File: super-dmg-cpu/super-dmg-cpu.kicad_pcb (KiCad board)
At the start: 2 copper layers, 83 x 78.5 mm, 61 parts, among them CN1 SCREEN, CN2 CART, CN3 BATTERY, CN4 BATTERY, P1 CART SHIELD GND PADS, P2 GND PAD, P3 GND PAD, P4 GND PAD, SW1 DPDT, U1 CPU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

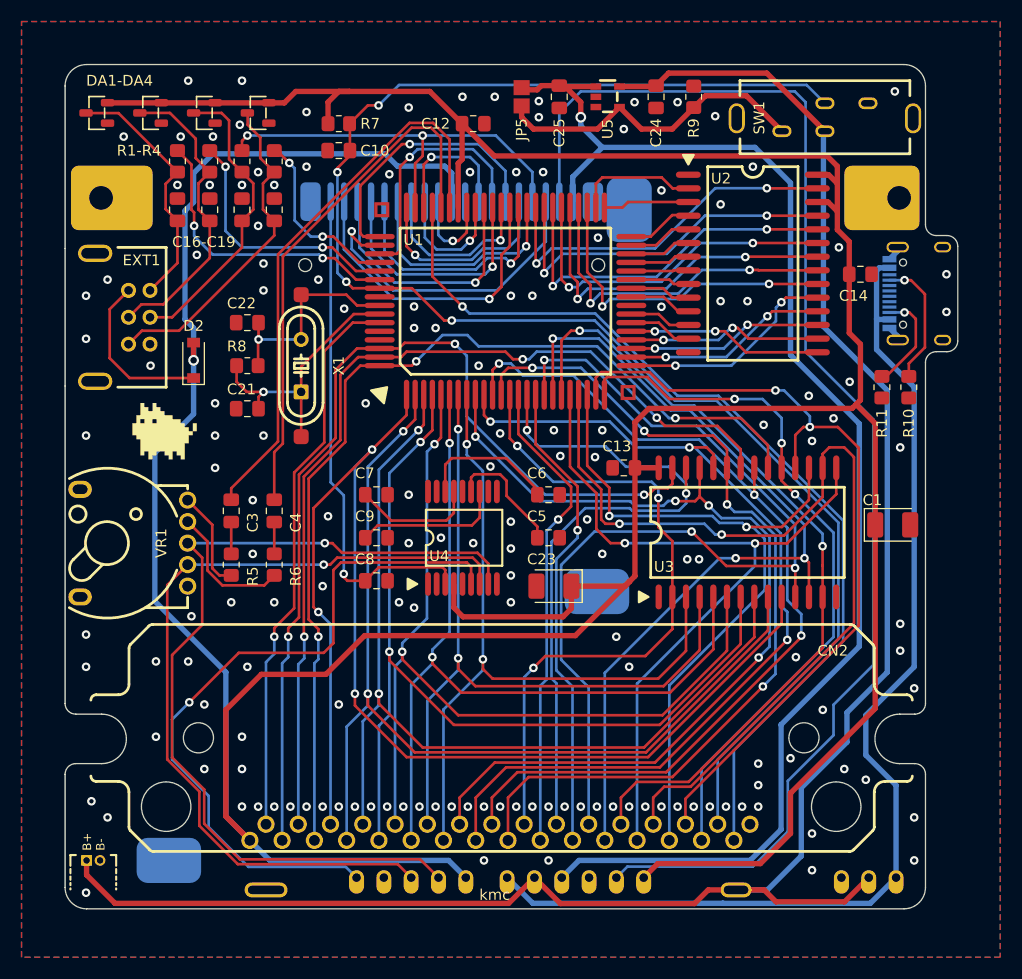
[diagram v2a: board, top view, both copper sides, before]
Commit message: CPU: clean up for DRC
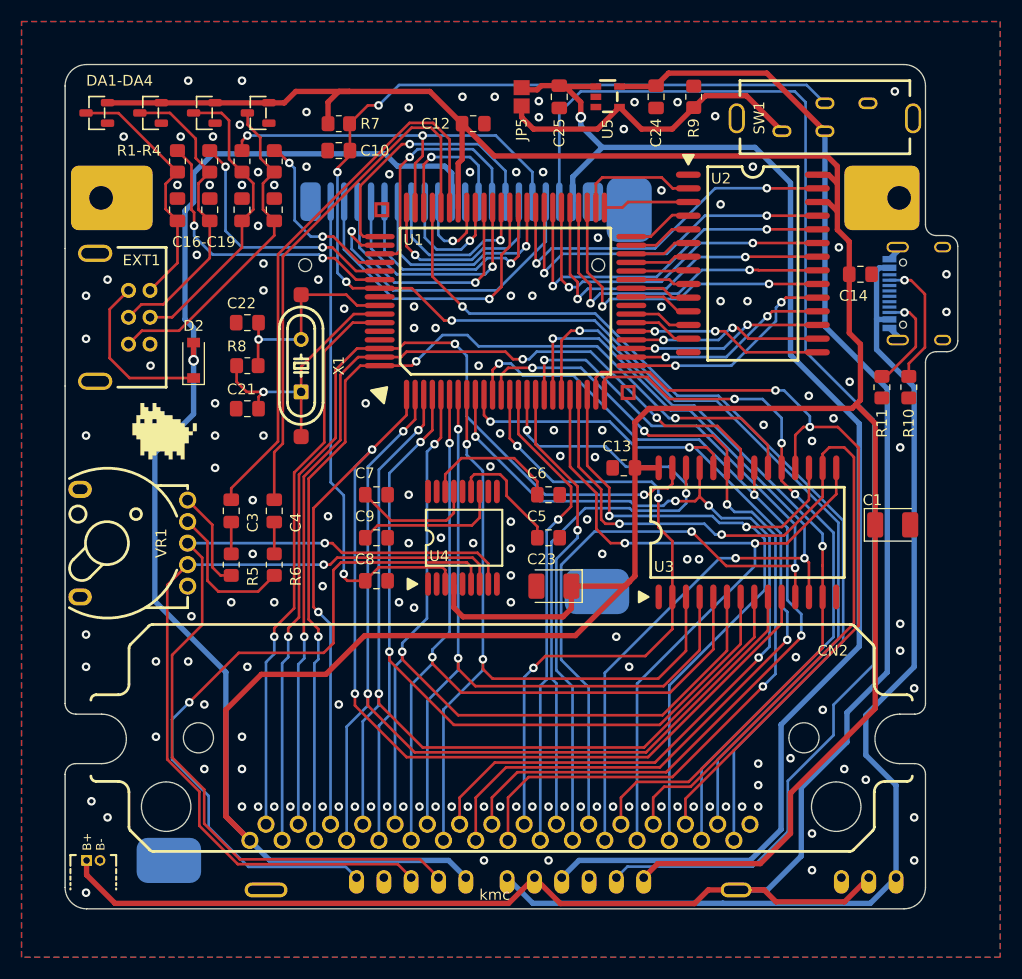
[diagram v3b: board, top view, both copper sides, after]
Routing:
- net Net-(R6-Pad2): track 12.5 -> 13.5 mm
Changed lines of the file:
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@@
     (fp_line (start -6 5) (end -5.031 5) (layer "F.SilkS") (width 0.254))
     (fp_arc (start -2.5 4) (mid -6.581538 -0.183962) (end -6 -6) (layer "F.SilkS") (width 0.254))
-    (fp_arc (start 6 -6) (mid 6.581539 -0.183961) (end 2.5 4) (layer "F.SilkS") (width 0.254))
+    (fp_arc (start 6 -6) (mid 6.581539 -0.183962) (end 2.5 4) (layer "F.SilkS") (width 0.254))
     (fp_arc (start -3.199638 -4.100525) (mid -3.096245 -5.695327) (end -1.501 -5.599) (layer "F.SilkS") (width 0.254))
     (fp_circle (center 0 -2.5) (end 2 -2.5) (layer "F.SilkS") (width 0.254) (fill none))
@@
   (segment (start 105.503135 49.651323) (end 105.501323 49.651323) (width 0.5) (layer "B.Cu") (net 16))
   (segment (start 105.551812 49.7) (end 105.503135 49.651323) (width 0.5) (layer "B.Cu") (net 16))
-  (segment (start 40 90.418296) (end 42.986489 93.404785) (width 0.25) (layer "F.Cu") (net 17))
-  (segment (start 42.8 78.1) (end 40 80.9) (width 0.25) (layer "F.Cu") (net 17))
-  (segment (start 41.445597 70.5) (end 42.8 71.854403) (width 0.25) (layer "F.Cu") (net 17))
-  (segment (start 63.07 99.9) (end 64.77 101.6) (width 0.25) (layer "F.Cu") (net 17))
   (segment (start 55.8 71.4) (end 68.4 71.4) (width 0.25) (layer "F.Cu") (net 17))
   (segment (start 69.4 72.4) (end 69.4 74.3) (width 0.25) (layer "F.Cu") (net 17))
-  (segment (start 54.9 70.5) (end 55.8 71.4) (width 0.25) (layer "F.Cu") (net 17))
   (segment (start 42.8 71.854403) (end 42.8 78.1) (width 0.25) (layer "F.Cu") (net 17))
+  (segment (start 54.9 70.5) (end 55.8 71.4) (width 0.25) (layer "F.Cu") (net 17))
   (segment (start 68.4 71.4) (end 69.4 72.4) (width 0.25) (layer "F.Cu") (net 17))
+  (segment (start 40 80.9) (end 40 90.418296) (width 0.25) (layer "F.Cu") (net 17))
   (segment (start 54.2 70.5) (end 54.9 70.5) (width 0.25) (layer "F.Cu") (net 17))
-  (segment (start 42.986489 96.586489) (end 46.3 99.9) (width 0.25) (layer "F.Cu") (net 17))
   (segment (start 46.3 99.9) (end 63.07 99.9) (width 0.25) (layer "F.Cu") (net 17))
+  (segment (start 42.8 78.1) (end 40 80.9) (width 0.25) (layer "F.Cu") (net 17))
+  (segment (start 42.986489 96.586489) (end 46.3 99.9) (width 0.25) (layer "F.Cu") (net 17))
+  (segment (start 63.07 99.9) (end 64.77 101.6) (width 0.25) (layer "F.Cu") (net 17))
+  (segment (start 40 90.418296) (end 42.986489 93.404785) (width 0.25) (layer "F.Cu") (net 17))
+  (segment (start 41.445597 70.5) (end 42.8 71.854403) (width 0.25) (layer "F.Cu") (net 17))
   (segment (start 42.986489 93.404785) (end 42.986489 96.586489) (width 0.25) (layer "F.Cu") (net 17))
-  (segment (start 40 80.9) (end 40 90.418296) (width 0.25) (layer "F.Cu") (net 17))
   (via (at 54.2 70.5) (size 0.8) (drill 0.4) (layers "F.Cu" "B.Cu") (net 17))
   (segment (start 54.2 70.5) (end 41.445597 70.5) (width 0.25) (layer "B.Cu") (net 17))
@@
   (segment (start 71.1 66.1) (end 71.1 64.7) (width 0.25) (layer "F.Cu") (net 75))
   (segment (start 71.1 64.7) (end 70.5 64.1) (width 0.25) (layer "F.Cu") (net 75))
-  (segment (start 71.0625 62.6) (end 66 62.6) (width 0.25) (layer "F.Cu") (net 76))
-  (segment (start 66 62.6) (end 65.4 63.2) (width 0.25) (layer "F.Cu") (net 76))
-  (segment (start 73.9625 65.5) (end 71.0625 62.6) (width 0.25) (layer "F.Cu") (net 76))
-  (segment (start 65.4 63.2) (end 65.4 65.7) (width 0.25) (layer "F.Cu") (net 76))
+  (segment (start 71.8 62.6) (end 73.9625 64.7625) (width 0.25) (layer "F.Cu") (net 76))
+  (segment (start 65.4 65.7) (end 65.4 64.1) (width 0.25) (layer "F.Cu") (net 76))
+  (segment (start 66.9 62.6) (end 71.8 62.6) (width 0.25) (layer "F.Cu") (net 76))
+  (segment (start 73.9625 64.7625) (end 73.9625 66) (width 0.25) (layer "F.Cu") (net 76))
+  (segment (start 65.4 64.1) (end 66.9 62.6) (width 0.25) (layer "F.Cu") (net 76))
   (segment (start 96.6505 48.1) (end 97.0755 47.675) (width 0.25) (layer "F.Cu") (net 77))
   (segment (start 86.8 54) (end 82.7 54) (width 0.25) (layer "F.Cu") (net 77))
@@
   (segment (start 40 86.9) (end 40 90.6) (width 0.25) (layer "B.Cu") (net 101))
   (segment (start 43.737347 68.79175) (end 41.445597 66.5) (width 0.25) (layer "F.Cu") (net 102))
-  (segment (start 43.737347 72.837347) (end 43.737347 68.79175) (width 0.25) (layer "F.Cu") (net 102))
-  (segment (start 44.4 73.5) (end 43.737347 72.837347) (width 0.25) (layer "F.Cu") (net 102))
-  (segment (start 45.5 73.5) (end 44.4 73.5) (width 0.25) (layer "F.Cu") (net 102))
+  (segment (start 43.737347 72.737347) (end 43.737347 68.79175) (width 0.25) (layer "F.Cu") (net 102))
+  (segment (start 44.5 73.5) (end 43.737347 72.737347) (width 0.25) (layer "F.Cu") (net 102))
+  (segment (start 45.5 73.5) (end 44.5 73.5) (width 0.25) (layer "F.Cu") (net 102))
   (segment (start 43.287347 70.34175) (end 41.445597 68.5) (width 0.25) (layer "F.Cu") (net 103))
-  (segment (start 44.675 74.425) (end 43.287347 73.037347) (width 0.25) (layer "F.Cu") (net 103))
-  (segment (start 48.575 74.425) (end 44.675 74.425) (width 0.25) (layer "F.Cu") (net 103))
-  (segment (start 49.5 73.5) (end 48.575 74.425) (width 0.25) (layer "F.Cu") (net 103))
-  (segment (start 43.287347 73.037347) (end 43.287347 70.34175) (width 0.25) (layer "F.Cu") (net 103))
+  (segment (start 49.5 73.5) (end 48 75) (width 0.25) (layer "F.Cu") (net 103))
+  (segment (start 44.3 75) (end 43.287347 73.987347) (width 0.25) (layer "F.Cu") (net 103))
+  (segment (start 48 75) (end 44.3 75) (width 0.25) (layer "F.Cu") (net 103))
+  (segment (start 43.287347 73.987347) (end 43.287347 70.34175) (width 0.25) (layer "F.Cu") (net 103))
   (segment (start 108.1 46.05) (end 108.7 46.05) (width 0.25) (layer "F.Cu") (net 104))
   (segment (start 110 47.35) (end 110 52.3) (width 0.25) (layer "F.Cu") (net 104))
@@
   (segment (start 73.6 32) (end 79.55 32) (width 0.5) (layer "F.Cu") (net 107))
   (segment (start 32.05 101.35) (end 32.05 100) (width 0.5) (layer "F.Cu") (net 108))
+  (segment (start 95.3 26.8) (end 100.7 32.2) (width 0.5) (layer "F.Cu") (net 108))
   (segment (start 73.69 101.6) (end 71.297501 103.992499) (width 0.5) (layer "F.Cu") (net 108))
   (segment (start 102.525489 103.849511) (end 104.775 101.6) (width 0.5) (layer "F.Cu") (net 108))
-  (segment (start 95.3 26.8) (end 86.1625 26.8) (width 0.5) (layer "F.Cu") (net 108))
   (segment (start 89.846569 102.742979) (end 88.576548 104.013) (width 0.5) (layer "F.Cu") (net 108))
-  (segment (start 100.668639 32.168639) (end 95.3 26.8) (width 0.5) (layer "F.Cu") (net 108))
   (segment (start 95.049547 102.742979) (end 96.156079 103.849511) (width 0.5) (layer "F.Cu") (net 108))
   (segment (start 92.436116 102.742979) (end 95.049547 102.742979) (width 0.5) (layer "F.Cu") (net 108))
@@
   (segment (start 81.6 28.05) (end 84.9125 28.05) (width 0.5) (layer "F.Cu") (net 108))
   (segment (start 92.436116 102.742979) (end 89.846569 102.742979) (width 0.5) (layer "F.Cu") (net 108))
-  (segment (start 100.668639 32.139193) (end 100.668639 32.168639) (width 0.5) (layer "F.Cu") (net 108))
+  (segment (start 95.3 26.8) (end 86.1625 26.8) (width 0.5) (layer "F.Cu") (net 108))
   (segment (start 88.576548 104.013) (end 76.103 104.013) (width 0.5) (layer "F.Cu") (net 108))
   (segment (start 96.156079 103.849511) (end 102.525489 103.849511) (width 0.5) (layer "F.Cu") (net 108))
-  (segment (start 98.5 99.6) (end 95.357021 102.742979) (width 0.5) (layer "B.Cu") (net 108))
   (segment (start 102.75 86.25) (end 102.75 89) (width 0.5) (layer "B.Cu") (net 108))
   (segment (start 106.5 82.5) (end 102.75 86.25) (width 0.5) (layer "B.Cu") (net 108))
-  (segment (start 95.357021 102.742979) (end 92.436116 102.742979) (width 0.5) (layer "B.Cu") (net 108))
-  (segment (start 100.561834 32.245998) (end 100.561834 50.361834) (width 0.5) (layer "B.Cu") (net 108))
-  (segment (start 106.5 56.3) (end 106.5 82.5) (width 0.5) (layer "B.Cu") (net 108))
-  (segment (start 102.75 89) (end 98.5 93.25) (width 0.5) (layer "B.Cu") (net 108))
   (segment (start 98.5 93.25) (end 98.5 99.6) (width 0.5) (layer "B.Cu") (net 108))
-  (segment (start 100.561834 50.361834) (end 106.5 56.3) (width 0.5) (layer "B.Cu") (net 108))
+  (segment (start 100.7 50.35) (end 106.5 56.15) (width 0.5) (layer "B.Cu") (net 108))
+  (segment (start 102.75 89) (end 98.5 93.25) (width 0.5) (layer "B.Cu") (net 108))
+  (segment (start 95.357021 102.742979) (end 92.436116 102.742979) (width 0.5) (layer "B.Cu") (net 108))
+  (segment (start 106.5 56.15) (end 106.5 82.5) (width 0.5) (layer "B.Cu") (net 108))
+  (segment (start 98.5 99.6) (end 95.357021 102.742979) (width 0.5) (layer "B.Cu") (net 108))
+  (segment (start 100.7 32.2) (end 100.7 50.35) (width 0.5) (layer "B.Cu") (net 108))
   (segment (start 78 29.5) (end 76.4625 27.9625) (width 0.5) (layer "F.Cu") (net 109))
   (segment (start 74.336109 27.9625) (end 76 27.9625) (width 0.5) (layer "F.Cu") (net 109))

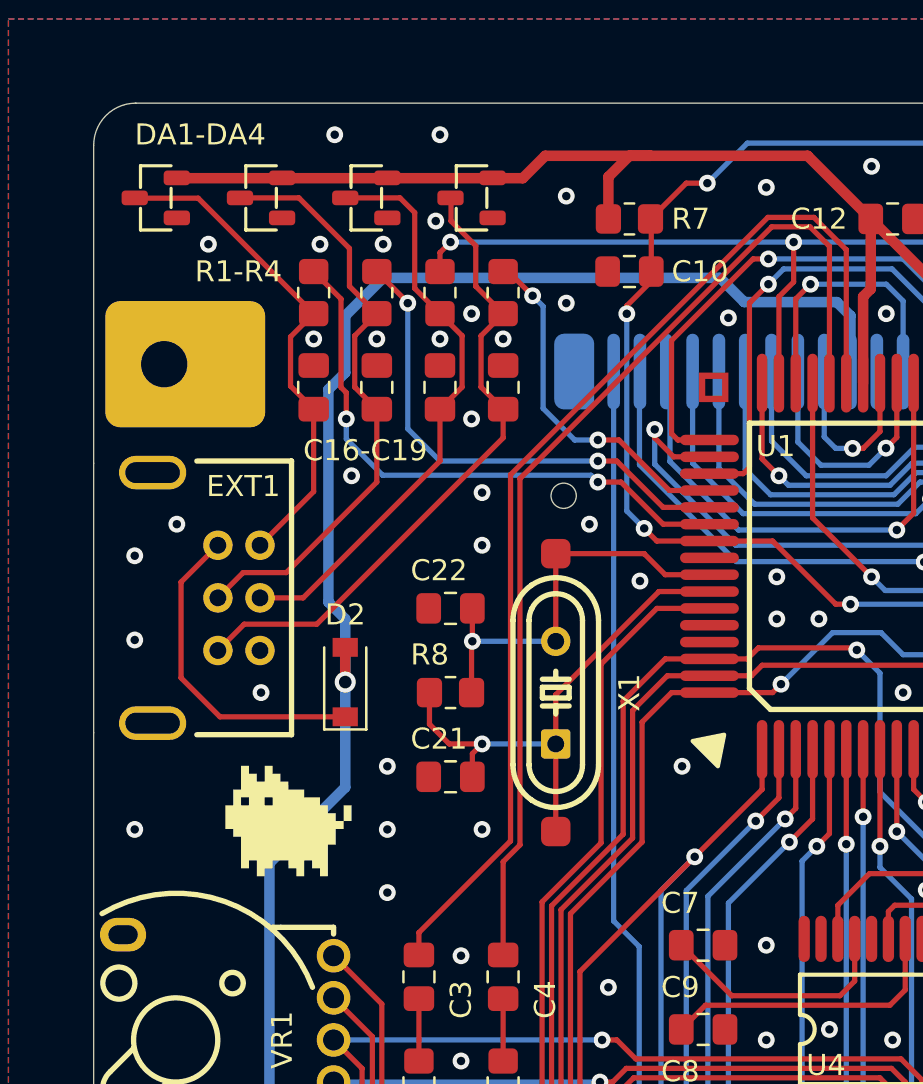
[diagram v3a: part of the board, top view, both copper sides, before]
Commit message: Fixed the link port  - The link port footprint was flipped
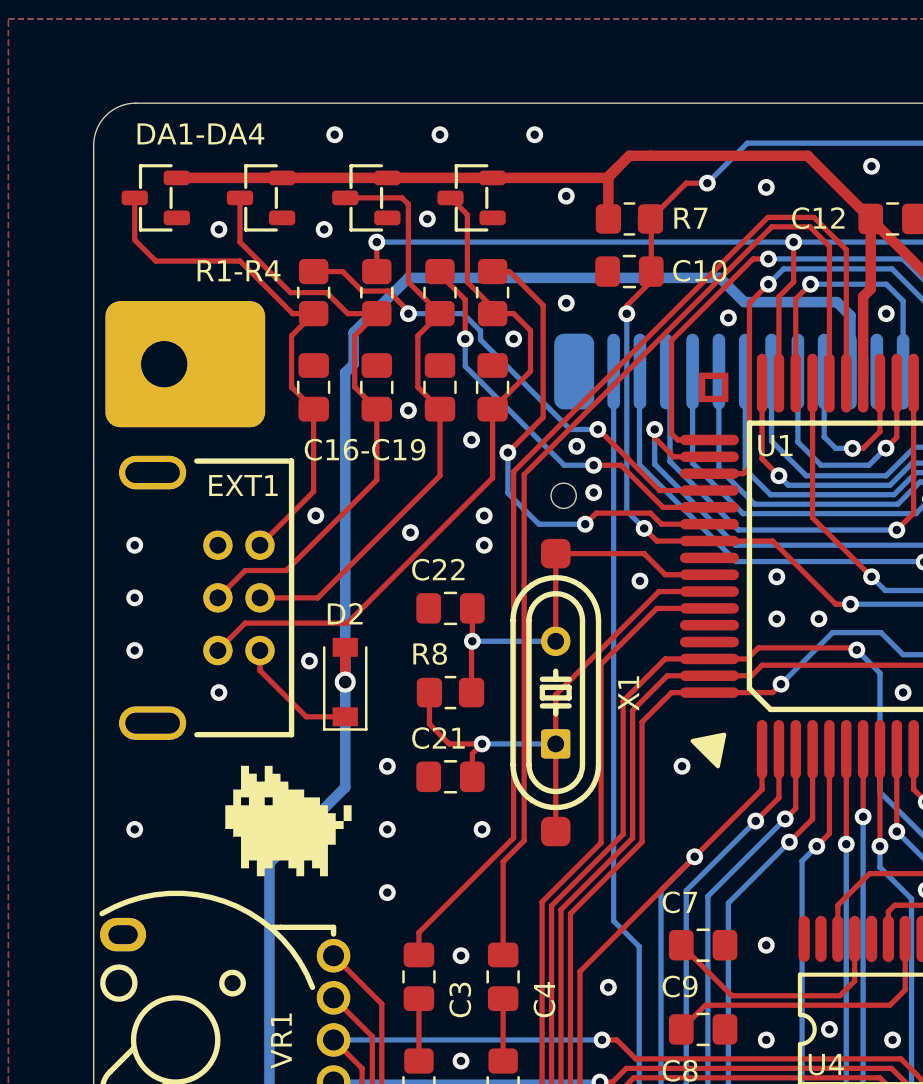
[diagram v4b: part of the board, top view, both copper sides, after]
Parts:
- moved DA2 15.0 mm to (33.0, 30.5)
- moved DA4 15.0 mm to (48.0, 30.5)
- moved C17 9.00 mm to (40.5, 39.5)
- moved R2 9.00 mm to (40.5, 35.0)
- moved C19 8.50 mm to (49.0, 39.5)
- moved R4 8.50 mm to (49.0, 35.0)
- moved DA1 5.00 mm to (38.0, 30.5)
- moved DA3 5.00 mm to (43.0, 30.5)
- moved C16 3.00 mm to (43.5, 39.5)
- moved C18 3.00 mm to (46.5, 39.5)
- moved R1 3.00 mm to (43.5, 35.0)
- moved R3 3.00 mm to (46.5, 35.0)
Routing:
- net Net-(D2-Pad1): track 15.6 -> 5.91 mm
- net /EXT_OUT: track 23.7 -> 32.7 mm
- net /SCK: track 16.7 -> 23.4 mm
- net /EXT_CLK: track 30.5 -> 24.9 mm
- net /SIN: track 24.0 -> 19.4 mm
- net /SOUT: track 27.5 -> 23.3 mm
- net /P14: track 39.3 -> 42.5 mm
- net +5V: track 404.9 -> 401.7 mm
- net /EXT_SD: track 27.9 -> 28.6 mm

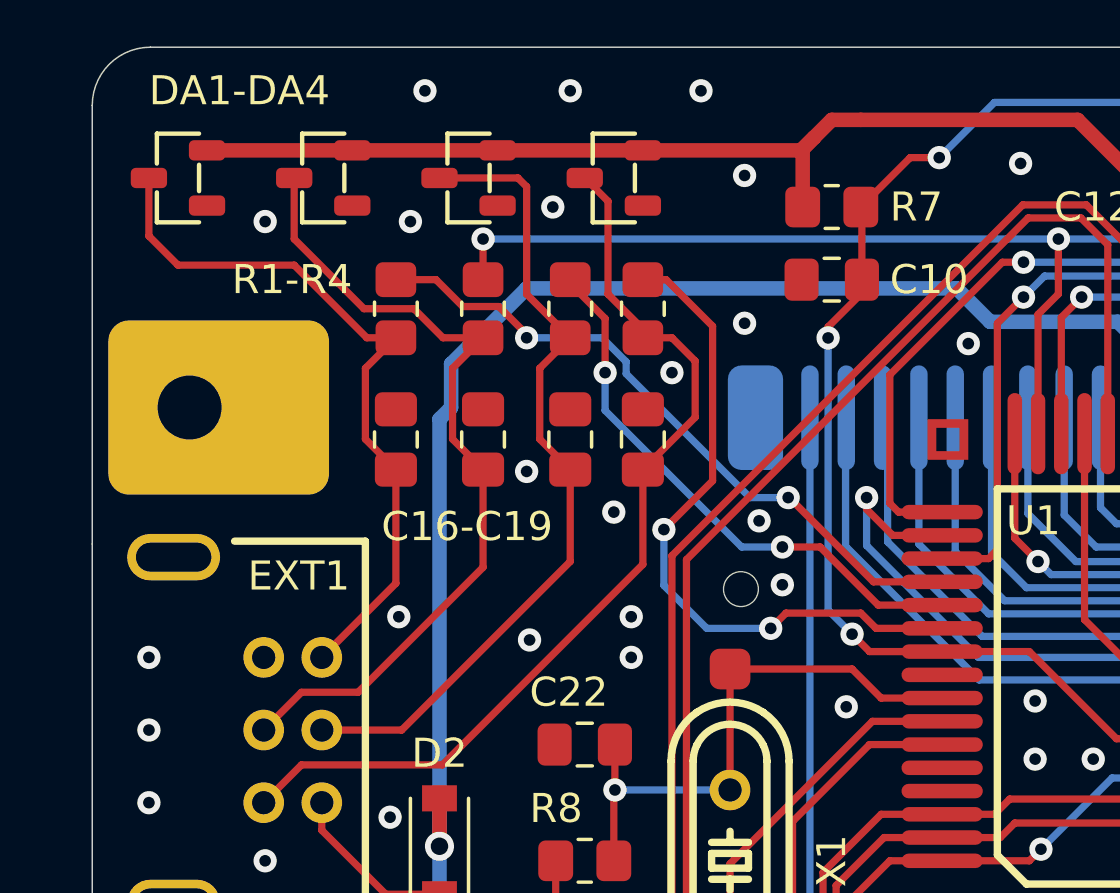
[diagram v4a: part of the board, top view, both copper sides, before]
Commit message: finished preliminary update to kicad 7
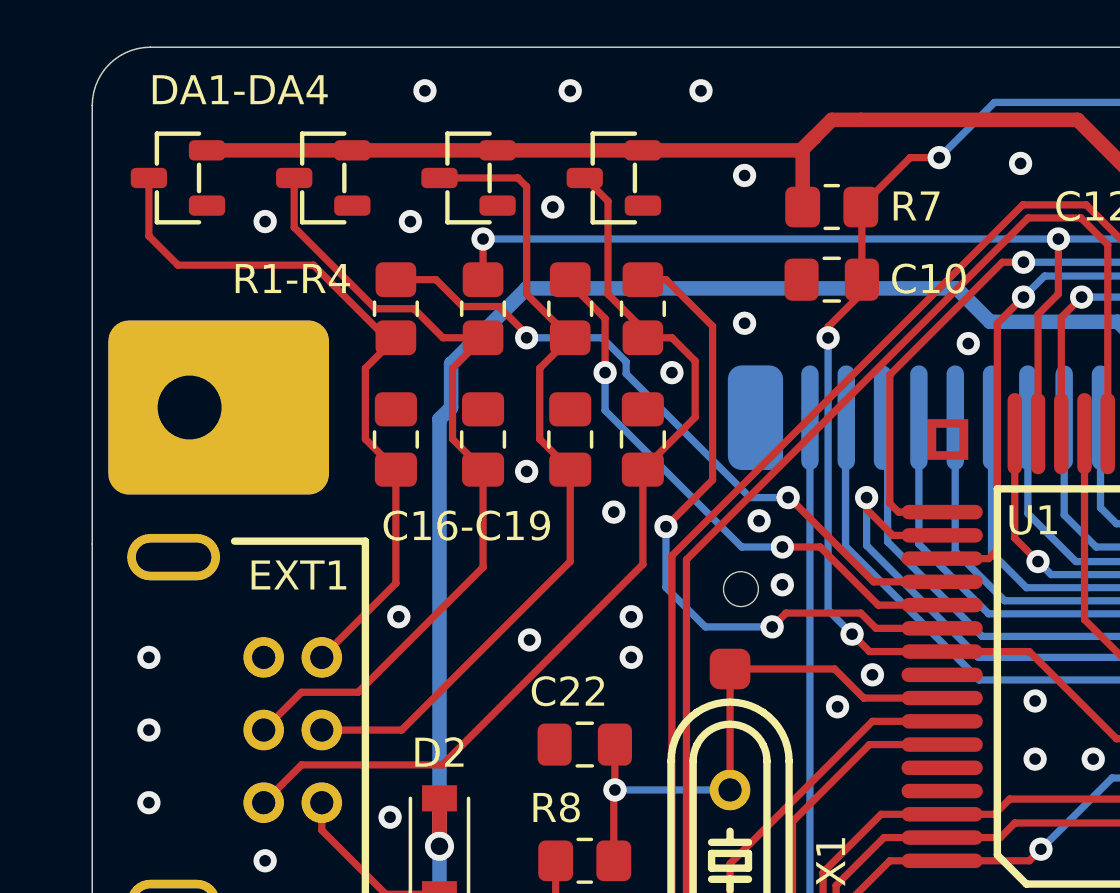
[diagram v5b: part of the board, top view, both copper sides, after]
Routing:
- net GND: vias 157 -> 158

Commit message: preparing for gerbers release
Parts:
- moved D2 0.15 mm to (42.0, 53.6), turned to -90 degrees
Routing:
- net Net-(D2-K): track 5.91 -> 4.05 mm
- net /SIN: track 19.4 -> 18.5 mm
- net GND: vias 158 -> 159

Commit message: v1.9
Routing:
- net GND: vias 159 -> 162
